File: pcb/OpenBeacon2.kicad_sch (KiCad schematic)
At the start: 47 parts, among them J1 Bias V, J11 BNC, J16 SMA CLKIN, J2 PAI+, J3 PAI-, J6 SMA, J9 GND, Q1 2N7002, Q2 MMBT4403, Q3 2SK3074, U1 TLV61046A, U2 ASTX-H11-25.000MHZ-T, U3 SN74LVC1G17, U4 SI5351C-B-GMR, U5 MCP4725A1T-E/CH

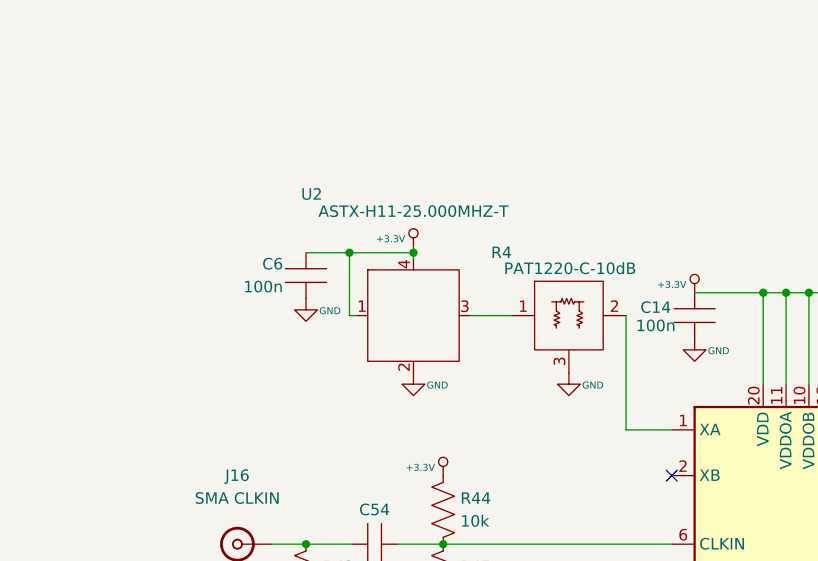
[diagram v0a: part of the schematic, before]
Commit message: TCXO: match Si5351BCBreakout 805bde2 (YXC OW2EL89CENUXK7YLC-25M, R4 10R feed, R13 0R DNP OE, C12 100n series to XA); remove PAT1220 pad
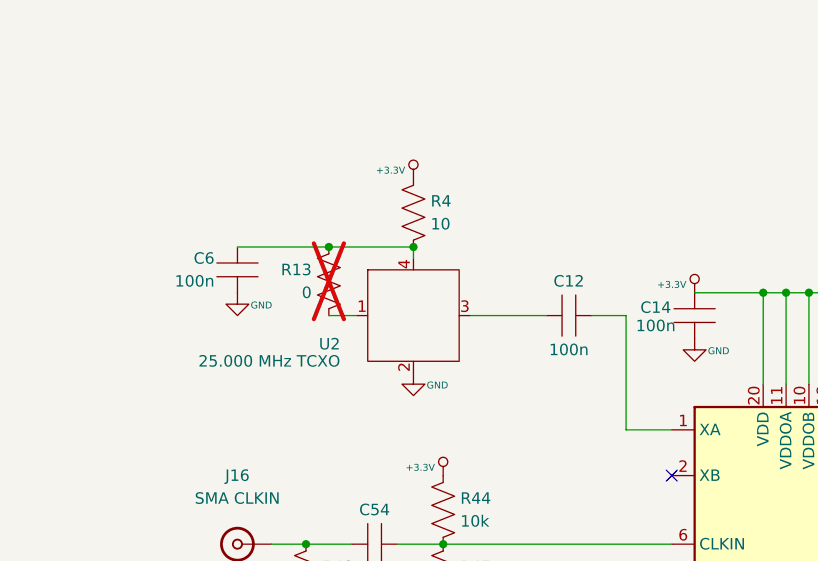
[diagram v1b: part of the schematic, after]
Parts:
- removed R4: PAT1220-C-10dB, EtherkitKicadLibrary:PAT1220, symbol EtherkitKicadLibrary:ChipAttenuator
- added C12: 100n, Capacitor_SMD:C_0805_2012Metric, symbol EtherkitKicadLibrary:C
- added R13: 0, Resistor_SMD:R_0805_2012Metric, symbol EtherkitKicadLibrary:R
- added R4: 10, Resistor_SMD:R_0805_2012Metric, symbol EtherkitKicadLibrary:R
- U2: value ASTX-H11-25.000MHZ-T -> 25.000 MHz TCXO; LCSC (none) -> C48888230; MPN (none) -> OW2EL89CENUXK7YLC-25M; Manufacturer (none) -> YXC
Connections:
- net +3.3V: now also R4.1; no longer C6.1, U2.1 (OE), U2.4 (VDD)
- net at U2.3 (OUT): now also C12.1
- net at U4.1 (XA): now also C12.2
- new net: R13.2, U2.1 (OE)
- new net: C6.1, R13.1, R4.2, U2.4 (VDD)
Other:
- moved on the sheet: C6

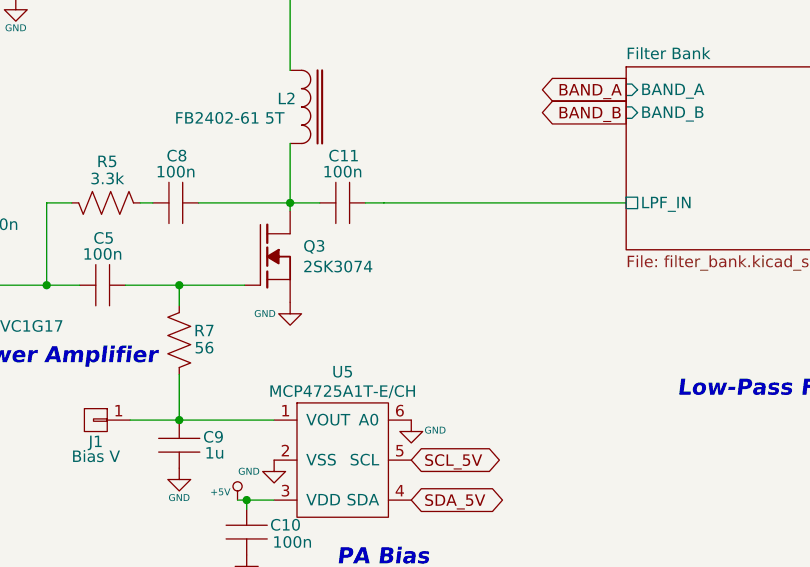
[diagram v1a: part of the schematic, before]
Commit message: PA: replace EOL 2SK3074 Q3 with 2x onsemi BS170 (Q3, Q8; TO-92, DNP, hand-solder) in parallel, 10R gate stoppers R16/R17
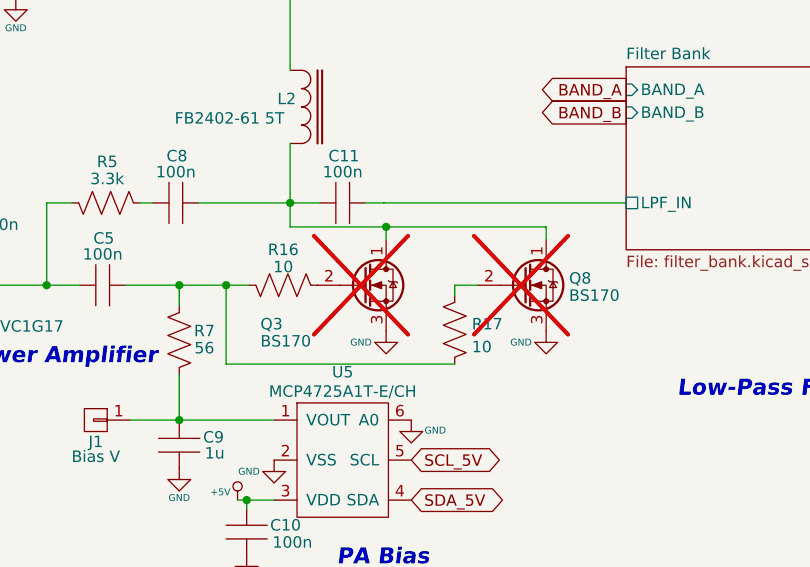
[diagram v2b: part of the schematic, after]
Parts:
- removed Q3: 2SK3074, EtherkitKicadLibrary:SOT89-3, symbol EtherkitKicadLibrary:MOS_N
- added Q3, Q8: BS170, Package_TO_SOT_THT:TO-92_Inline, symbol Transistor_FET:BS170
- added R16, R17: 10, Resistor_SMD:R_0603_1608Metric, symbol EtherkitKicadLibrary:R
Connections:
- net GND: now also Q3.3 (S), Q8.3 (S)
- net at C5.1, R7.1: now also R16.1, R17.2
- net at C11.2, C8.1, L2.2: now also Q3.1 (D), Q8.1 (D)
- new net: Q3.2 (G), R16.2
- new net: Q8.2 (G), R17.1

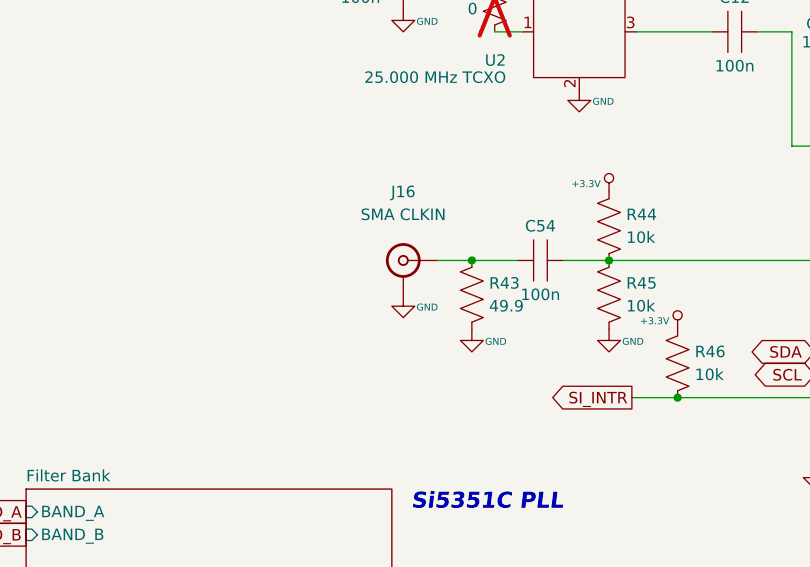
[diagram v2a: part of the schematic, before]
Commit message: ESD: SP0503BAHT (C7074) on J8 I2C (D19) and J10 UART (D20) with 220R series R76-R79 (C17557), header-side nets HDR_SCL/SDA/RX/TX; ESD5V3U1U-02LRH (C3011174) D21 on J16 CLKIN SMA, net CLKIN_SMA; regen PDF
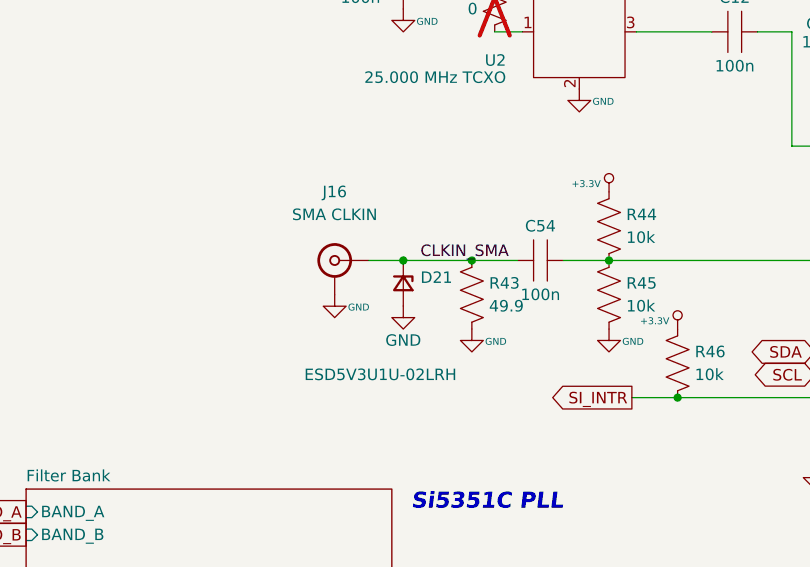
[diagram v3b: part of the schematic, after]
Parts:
- added D21: ESD5V3U1U-02LRH, Diode_SMD:D_SOD-882, symbol Device:D_Zener_Small
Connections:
- net GND: now also D21.2 (A)
- net CLKIN_SMA: now reaches C54.1, J16.1 (In), R43.1
- net CLKIN_SMA: now also D21.1 (K)
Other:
- moved on the sheet: J16
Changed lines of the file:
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@@
 	(symbol
 		(lib_id "EtherkitKicadLibrary:BNC")
-		(at 167.64 73.66 0)
+		(at 160.02 73.66 0)
 		(mirror y)
 		(unit 1)
@@
 		(dnp no)
 		(property "Reference" "J16"
-			(at 167.64 66.04 0)
+			(at 160.02 66.04 0)
 			(effects
 				(font
@@
 		)
 		(property "Value" "SMA CLKIN"
-			(at 167.64 68.58 0)
+			(at 160.02 68.58 0)
 			(effects
 				(font
@@
 		)
 		(property "Footprint" "OB2:SMA-ENDLAUNCH"
-			(at 167.64 73.66 0)
+			(at 160.02 73.66 0)
 			(effects
 				(font
@@
 		)
 		(property "Datasheet" ""
-			(at 167.64 73.66 0)
+			(at 160.02 73.66 0)
 			(effects
 				(font
@@
 		)
 		(property "MPN" "BWSMA-KE-P001"
-			(at 167.64 73.66 0)
+			(at 160.02 73.66 0)
 			(effects
 				(font
@@
 		)
 		(property "Manufacturer" "BAT Wireless"
-			(at 167.64 73.66 0)
+			(at 160.02 73.66 0)
 			(effects
 				(font
@@
 		)
 		(property "LCSC" "C496550"
-			(at 167.64 73.66 0)
+			(at 160.02 73.66 0)
 			(effects
 				(font
@@
 		)
 		(property "Description" "SMA end-launch jack, 50 ohm, external reference into Si5351C CLKIN"
-			(at 167.64 73.66 0)
+			(at 160.02 73.66 0)
 			(effects
 				(font
@@
 	(symbol
 		(lib_id "OpenBeacon2-rescue:GND-OpenBeaconMini-rescue")
-		(at 167.64 77.47 0)
+		(at 160.02 77.47 0)
 		(unit 1)
 		(body_style 1)
@@
 		(dnp no)
 		(property "Reference" "#PWR0312"
-			(at 167.64 83.82 0)
+			(at 160.02 83.82 0)
 			(hide yes)
 			(show_name no)
@@
 		)
 		(property "Value" "GND"
-			(at 170.307 78.867 0)
+			(at 162.687 78.867 0)
 			(show_name no)
 			(do_not_autoplace no)
@@
 		)
 		(property "Footprint" ""
-			(at 167.64 77.47 0)
+			(at 160.02 77.47 0)
 			(hide yes)
 			(show_name no)
@@
 		)
 		(property "Datasheet" ""
-			(at 167.64 77.47 0)
+			(at 160.02 77.47 0)
 			(hide yes)
 			(show_name no)
@@
 		)
 		(property "Description" ""
-			(at 167.64 77.47 0)
+			(at 160.02 77.47 0)
 			(show_name no)
 			(do_not_autoplace no)
@@
 				)
 			)
-		)
-	)
-	(wire
-		(pts
-			(xy 171.45 73.66)
-			(xy 175.26 73.66)
-		)
-		(stroke
-			(width 0)
-			(type default)
 		)
 	)
@@
 		)
 	)
+	(wire
+		(pts
+			(xy 163.83 73.66) (xy 167.64 73.66)
+		)
+		(stroke
+			(width 0)
+			(type default)
+		)
+	)
+	(wire
+		(pts
+			(xy 167.64 73.66) (xy 175.26 73.66)
+		)
+		(stroke
+			(width 0)
+			(type default)
+		)
+	)
+	(junction
+		(at 167.64 73.66)
+		(diameter 0)
+		(color 0 0 0 0)
+	)
+	(symbol
+		(lib_id "Device:D_Zener_Small")
+		(at 167.64 76.2 270)
+		(unit 1)
+		(exclude_from_sim no)
+		(in_bom yes)
+		(on_board yes)
+		(dnp no)
+		(property "Reference" "D21"
+			(at 169.545 75.565 90)
+			(effects
+				(font
+					(size 1.27 1.27)
+				)
+				(justify left)
+			)
+		)
+		(property "Value" "ESD5V3U1U-02LRH"
+			(at 165.1 86.36 90)
+			(effects
+				(font
+					(size 1.27 1.27)
+				)
+			)
+		)
+		(property "Footprint" "Diode_SMD:D_SOD-882"
+			(at 167.64 76.2 0)
+			(effects
+				(font
+					(size 1.27 1.27)
+				)
+				(hide yes)
+			)
+		)
+		(property "Datasheet" ""
+			(at 167.64 76.2 0)
+			(effects
+				(font
+					(size 1.27 1.27)
+				)
+				(hide yes)
+			)
+		)
+		(property "MPN" "ESD5V3U1U-02LRH"
+			(at 167.64 76.2 0)
+			(effects
+				(font
+					(size 1.27 1.27)
+				)
+				(hide yes)
+			)
+		)
+		(property "Manufacturer" "Infineon"
+			(at 167.64 76.2 0)
+			(effects
+				(font
+					(size 1.27 1.27)
+				)
+				(hide yes)
+			)
+		)
+		(property "LCSC" "C3011174"
+			(at 167.64 76.2 0)
+			(effects
+				(font
+					(size 1.27 1.27)
+				)
+				(hide yes)
+			)
+		)
+		(pin "1"
+		)
+		(pin "2"
+		)
+		(instances
+			(project "OpenBeacon2"
+				(path "/046319a3-a6ce-4e59-a888-94e340127381"
+					(reference "D21")
+					(unit 1)
+				)
+			)
+		)
+	)
+	(symbol
+		(lib_id "OpenBeacon2-rescue:GND-OpenBeaconMini-rescue")
+		(at 167.64 78.74 0)
+		(unit 1)
+		(exclude_from_sim no)
+		(in_bom no)
+		(on_board yes)
+		(dnp no)
+		(property "Reference" "#PWR0947"
+			(at 167.64 82.55 0)
+			(effects
+				(font
+					(size 1.27 1.27)
+				)
+				(hide yes)
+			)
+		)
+		(property "Value" "GND"
+			(at 167.64 82.55 0)
+			(effects
+				(font
+					(size 1.27 1.27)
+				)
+			)
+		)
+		(property "Footprint" ""
+			(at 167.64 78.74 0)
+			(effects
+				(font
+					(size 1.27 1.27)
+				)
+				(hide yes)
+			)
+		)
+		(property "Datasheet" ""
+			(at 167.64 78.74 0)
+			(effects
+				(font
+					(size 1.27 1.27)
+				)
+				(hide yes)
+			)
+		)
+		(pin "1"
+		)
+		(instances
+			(project "OpenBeacon2"
+				(path "/046319a3-a6ce-4e59-a888-94e340127381"
+					(reference "#PWR0947")
+					(unit 1)
+				)
+			)
+		)
+	)
+	(label "CLKIN_SMA"
+		(at 169.545 73.66 0)
+		(effects
+			(font
+				(size 1.27 1.27)
+			)
+			(justify left bottom)
+		)
+	)

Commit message: D21 on J16 CLKIN_SMA: bidirectional PESD5V0F1BL,315 (Nexperia, C45961, 0.4pF, VRWM 5.5V) replaces unidirectional ESD5V3U1U; Device:D_TVS_Small, SOD-882; regen PDF
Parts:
- D21: value ESD5V3U1U-02LRH -> PESD5V0F1BL; symbol Device:D_Zener_Small -> Device:D_TVS_Small; LCSC C3011174 -> C45961; MPN ESD5V3U1U-02LRH -> PESD5V0F1BL,315; Manufacturer Infineon -> Nexperia
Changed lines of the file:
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@@
 	)
 	(symbol
-		(lib_id "Device:D_Zener_Small")
+		(lib_id "Device:D_TVS_Small")
 		(at 167.64 76.2 270)
 		(unit 1)
@@
 			)
 		)
-		(property "Value" "ESD5V3U1U-02LRH"
+		(property "Value" "PESD5V0F1BL"
 			(at 165.1 86.36 90)
 			(effects
@@
 			)
 		)
-		(property "Datasheet" ""
+		(property "Datasheet" "https://assets.nexperia.com/documents/data-sheet/PESD5V0F1BL.pdf"
 			(at 167.64 76.2 0)
 			(effects
@@
 			)
 		)
-		(property "MPN" "ESD5V3U1U-02LRH"
+		(property "MPN" "PESD5V0F1BL,315"
 			(at 167.64 76.2 0)
 			(effects
@@
 			)
 		)
-		(property "Manufacturer" "Infineon"
+		(property "Manufacturer" "Nexperia"
 			(at 167.64 76.2 0)
 			(effects
@@
 			)
 		)
-		(property "LCSC" "C3011174"
+		(property "LCSC" "C45961"
 			(at 167.64 76.2 0)
 			(effects

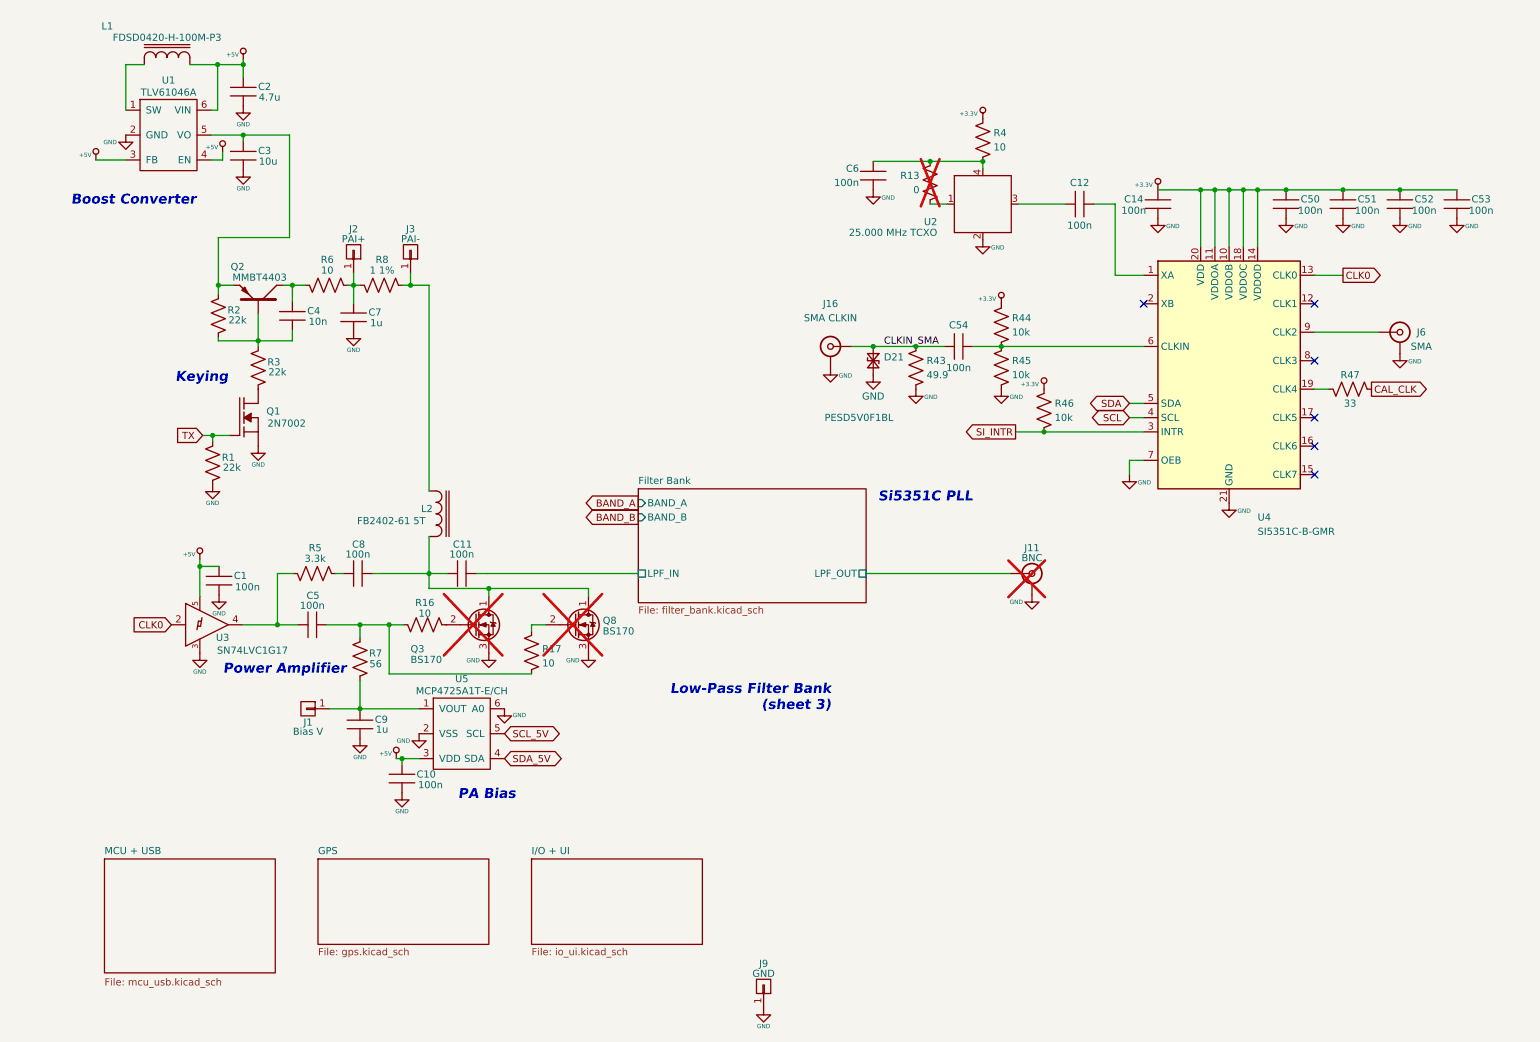
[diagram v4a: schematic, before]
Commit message: Schematic style: pages 1-2 (root, I/O+UI) functional blocks in dashed boxes with titles and notes, matching other sheets; Si5351C block up 12.7 mm, PA/bias/filter-bank band down 6.35 mm, boost down 2.54 mm, EEPROM moved right, OLED down 5.08 mm; no connectivity change (netlist identical); regen PDF
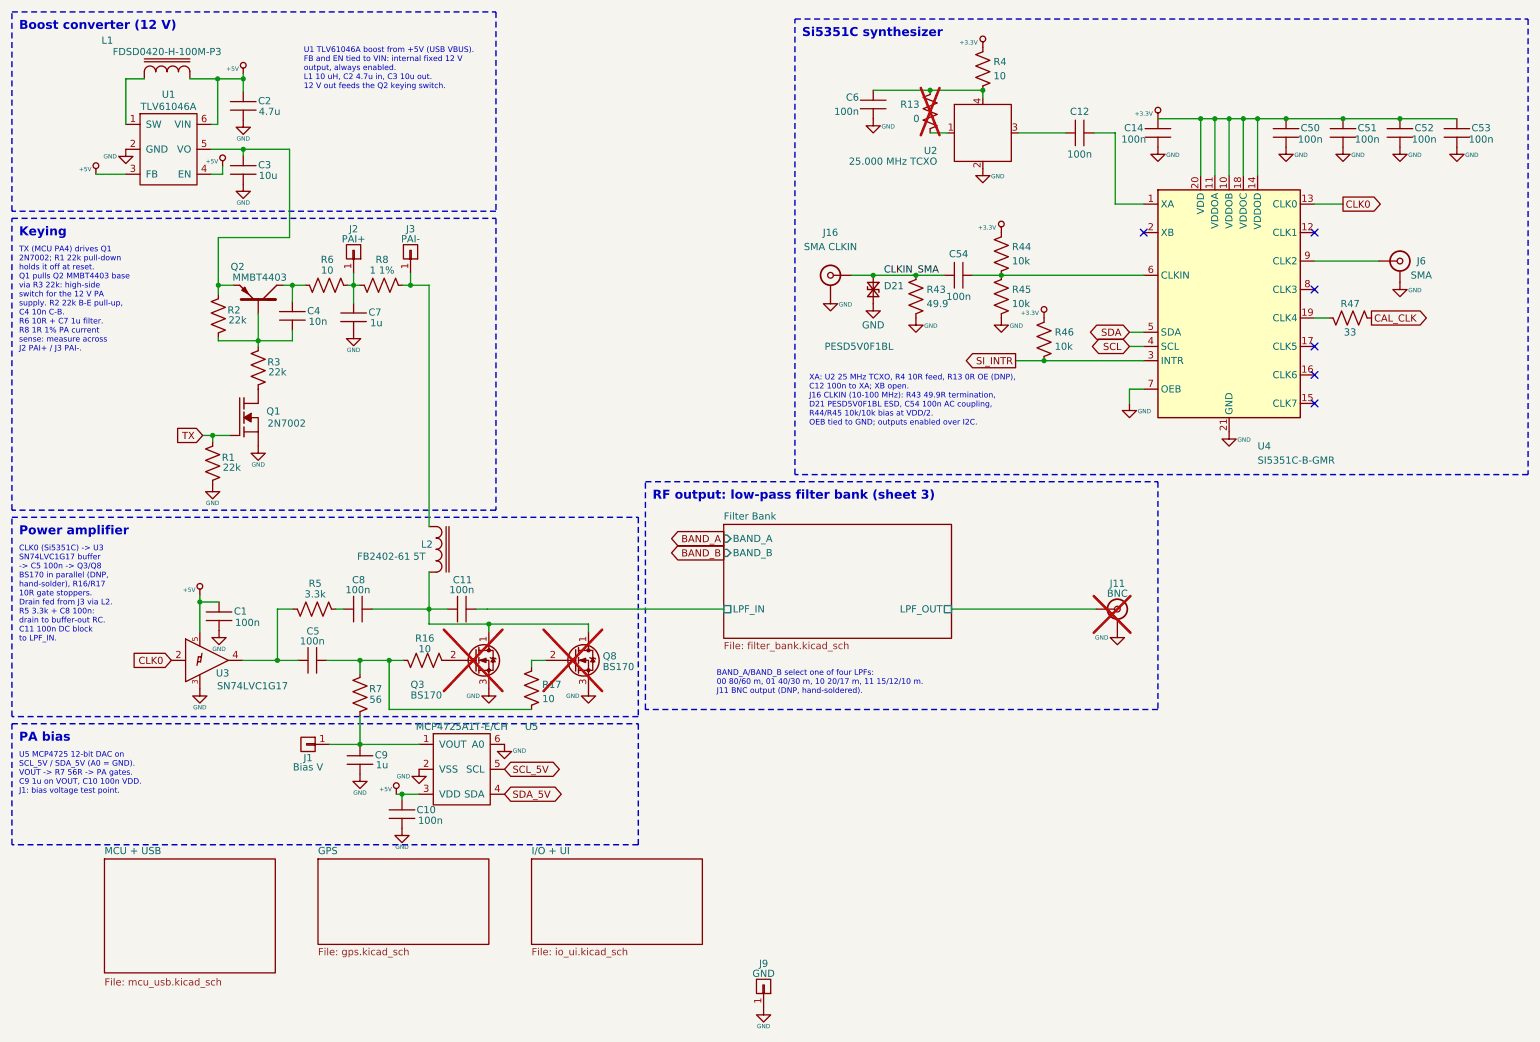
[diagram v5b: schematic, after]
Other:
- note added: "BAND_A/BAND_B select one of four LPFs: 00 80/60 m, 01 40/30 m, 10 20/17 m, 11 15/12/10 m. J11 BNC output (DNP, hand-soldered)."
- note added: "Boost converter (12 V)"
- note added: "CLK0 (Si5351C) -> U3 SN74LVC1G17 buffer -> C5 100n -> Q3/Q8 BS170 in parallel (DNP, hand-solder), R16/R17 10R gate stoppers. Drain fed from J3 via L2. R5 3.3k + C8 100n: drain to buffer-out RC. C11 100n DC block to LPF_IN."
- note added: "PA bias"
- note added: "Power amplifier"
- note added: "RF output: low-pass filter bank (sheet 3)"
- note added: "Si5351C synthesizer"
- note added: "TX (MCU PA4) drives Q1 2N7002; R1 22k pull-down holds it off at reset. Q1 pulls Q2 MMBT4403 base via R3 22k: high-side switch for the 12 V PA supply. R2 22k B-E pull-up, C4 10n C-B. R6 10R + C7 1u filter. R8 1R 1% PA current sense: measure across J2 PAI+ / J3 PAI-."
- note added: "U1 TLV61046A boost from +5V (USB VBUS). FB and EN tied to VIN: internal fixed 12 V output, always enabled. L1 10 uH, C2 4.7u in, C3 10u out. 12 V out feeds the Q2 keying switch."
- note added: "U5 MCP4725 12-bit DAC on SCL_5V / SDA_5V (A0 = GND). VOUT -> R7 56R -> PA gates. C9 1u on VOUT, C10 100n VDD. J1: bias voltage test point."
- note added: "XA: U2 25 MHz TCXO, R4 10R feed, R13 0R OE (DNP), C12 100n to XA; XB open. J16 CLKIN (10-100 MHz): R43 49.9R termination, D21 PESD5V0F1BL ESD, C54 100n AC coupling, R44/R45 10k/10k bias at VDD/2. OEB tied to GND; outputs enabled over I2C."
- note removed: "Boost Converter"
- note removed: "Low-Pass Filter Bank (sheet 3)"
- note removed: "PA Bias"
- note removed: "Power Amplifier"
- note removed: "Si5351C PLL"
- moved on the sheet: C1, C10, C11, C12, C14, C2, C3, C5, C50, C51, C52, C53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
